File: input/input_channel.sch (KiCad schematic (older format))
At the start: 4 parts

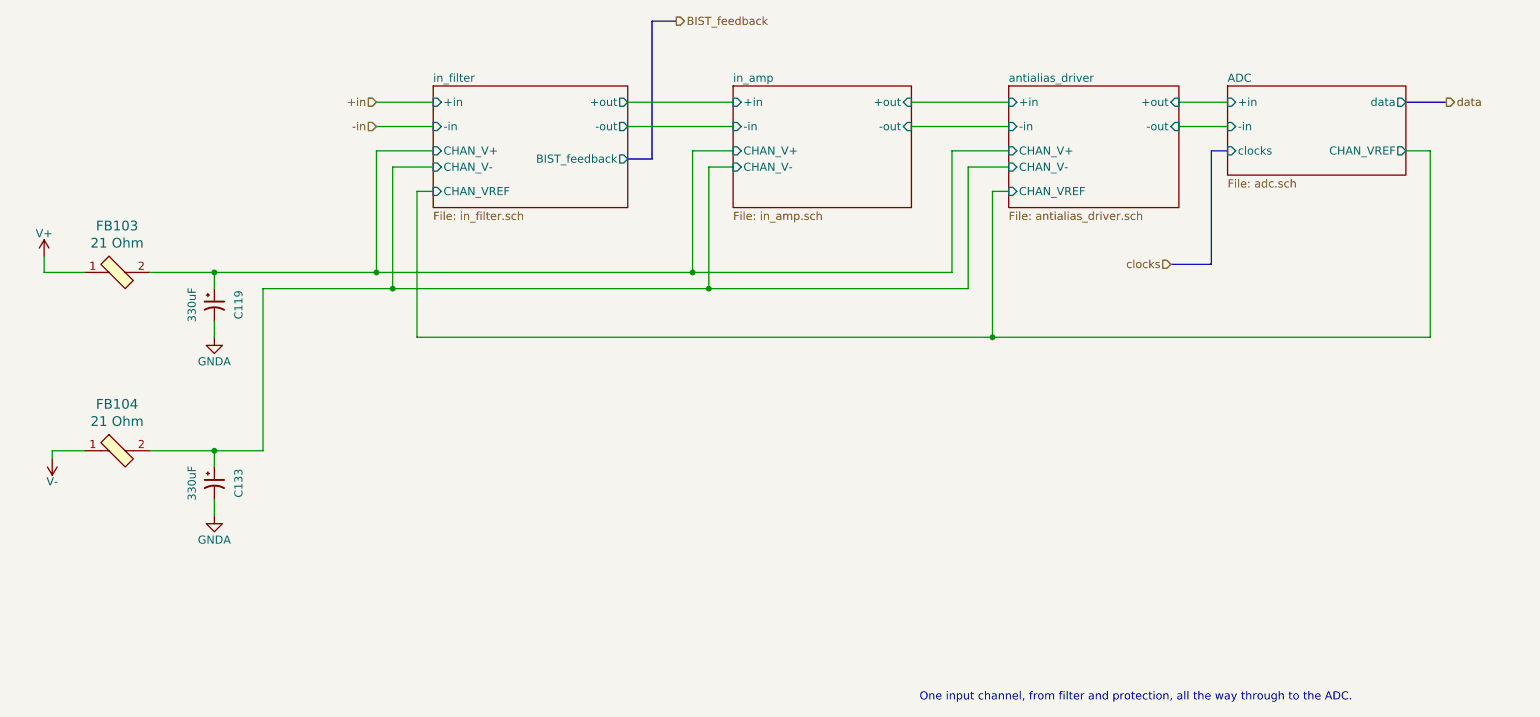
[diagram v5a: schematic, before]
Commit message: Cleanup to get ready to start board layout. I had to get rid off all the bus signals, since in Kicad busses don't work that way.  Added a couple testpoints; many more needed.
Work on component placement in PCB.  I changed DGND to plain GND and "protective earth" to
"earth" (for chassis ground).  Chassis ground is now connected on the board only via a capacitor.
I had to fix the connector footprint to match the pin numbers on the symbol (there was a case
difference).
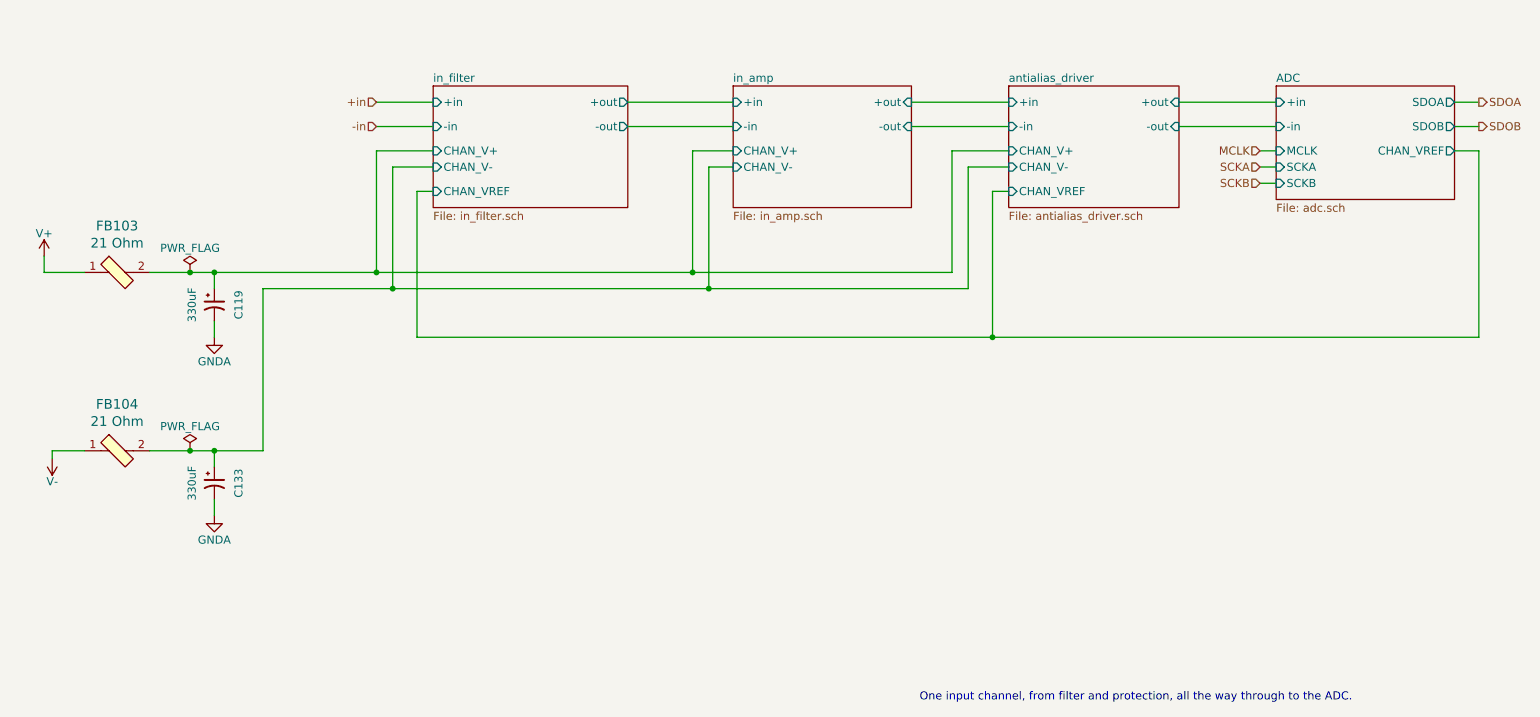
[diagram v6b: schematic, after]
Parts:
- FB103, FB104: footprint digikey-footprints:0805 -> Inductor_SMD:L_0805_2012Metric
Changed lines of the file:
@@
 F4 "-in" I L 4150 3200 50
 F5 "+in" I L 4150 3050 50
-F6 "BIST_feedback" O R 5350 3400 50
-F7 "CHAN_V+" I L 4150 3350 50
-F8 "CHAN_V-" I L 4150 3450 50
-F9 "CHAN_VREF" I L 4150 3600 50
+F6 "CHAN_V+" I L 4150 3350 50
+F7 "CHAN_V-" I L 4150 3450 50
+F8 "CHAN_VREF" I L 4150 3600 50
 $EndSheet
 $Sheet
@@
 F7 "CHAN_V-" I L 6000 3450 50
 $EndSheet
-Wire Wire Line
-	8750 3200 9050 3200
-Wire Wire Line
-	8750 3050 9050 3050
-Text HLabel 10400 3050 2    50   Output ~ 0
-data
 Text HLabel 3800 3050 0    50   Input ~ 0
 +in
@@
 Wire Wire Line
 	3800 3200 4150 3200
-Text HLabel 8700 4050 0    50   Input ~ 0
-clocks
-Wire Bus Line
-	9050 3350 8950 3350
-Wire Bus Line
-	8950 3350 8950 4050
-Wire Bus Line
-	8950 4050 8700 4050
-Wire Bus Line
-	10150 3050 10400 3050
-Wire Bus Line
-	5350 3400 5500 3400
-Wire Bus Line
-	5500 3400 5500 2550
-Wire Bus Line
-	5500 2550 5650 2550
 Wire Wire Line
 	7100 3050 7700 3050
@@
 F 0 "FB103" H 2200 4387 60  0000 C CNN
 F 1 "21 Ohm" H 2200 4281 60  0000 C CNN
-F 2 "digikey-footprints:0805" H 2400 4300 60  0001 L CNN
+F 2 "Inductor_SMD:L_0805_2012Metric" H 2400 4300 60  0001 L CNN
 F 3 "https://www.yuden.co.jp/productdata/catalog/chipbeads01_e.pdf" H 2400 4400 60  0001 L CNN
 F 4 "HZ0805C202R-10" H 2400 4600 60  0001 L CNN "MPN"
@@
 $EndComp
 Wire Wire Line
-	2400 4100 2800 4100
+	2400 4100 2650 4100
 Wire Wire Line
 	2800 4100 2800 4200
@@
 F 0 "FB104" H 2200 5487 60  0000 C CNN
 F 1 "21 Ohm" H 2200 5381 60  0000 C CNN
-F 2 "digikey-footprints:0805" H 2400 5400 60  0001 L CNN
+F 2 "Inductor_SMD:L_0805_2012Metric" H 2400 5400 60  0001 L CNN
 F 3 "https://www.yuden.co.jp/productdata/catalog/chipbeads01_e.pdf" H 2400 5500 60  0001 L CNN
 F 4 "HZ0805C202R-10" H 2400 5700 60  0001 L CNN "MPN"
@@
 $EndComp
 Wire Wire Line
-	2400 5200 2800 5200
+	2400 5200 2650 5200
 Wire Wire Line
 	2800 5200 2800 5300
@@
 	7450 3450 7700 3450
 Connection ~ 2800 5200
-Text HLabel 5650 2550 2    50   Output ~ 0
-BIST_feedback
 Wire Wire Line
 	5750 3350 5750 4100
@@
 	3900 4200 5850 4200
 $Sheet
-S 9050 2950 1100 550
+S 9350 2950 1100 700
 U 5DA78AA2
 F0 "ADC" 50
 F1 "adc.sch" 50
-F2 "+in" I L 9050 3050 50
-F3 "-in" I L 9050 3200 50
-F4 "data" O R 10150 3050 50
-F5 "clocks" I L 9050 3350 50
-F6 "CHAN_VREF" O R 10150 3350 50
+F2 "+in" I L 9350 3050 50
+F3 "-in" I L 9350 3200 50
+F4 "CHAN_VREF" O R 10450 3350 50
+F5 "SDOA" O R 10450 3050 50
+F6 "SDOB" O R 10450 3200 50
+F7 "MCLK" I L 9350 3350 50
+F8 "SCKB" I L 9350 3550 50
+F9 "SCKA" I L 9350 3450 50
 $EndSheet
 Wire Wire Line
@@
 Connection ~ 5850 4200
 Wire Wire Line
-	10150 3350 10300 3350
-Wire Wire Line
-	10300 3350 10300 4500
+	10450 3350 10600 3350
+Wire Wire Line
+	10600 3350 10600 4500
 Wire Wire Line
 	7700 3600 7600 3600
@@
 Connection ~ 7600 4500
 Wire Wire Line
-	7600 4500 10300 4500
-Wire Wire Line
 	4150 3600 4050 3600
 Wire Wire Line
 	4050 3600 4050 4500
+$Comp
+L power:PWR_FLAG #FLG0103
+U 1 1 5E8B0766
+P 2650 4100
+F 0 "#FLG0103" H 2650 4175 50  0001 C CNN
+F 1 "PWR_FLAG" H 2650 4250 50  0000 C CNN
+F 2 "" H 2650 4100 50  0001 C CNN
+F 3 "~" H 2650 4100 50  0001 C CNN
+	1    2650 4100
+	1    0    0    -1
+$EndComp
+Connection ~ 2650 4100
+Wire Wire Line
+	2650 4100 2800 4100
+$Comp
+L power:PWR_FLAG #FLG0104
+U 1 1 5E8B104C
+P 2650 5200
+F 0 "#FLG0104" H 2650 5275 50  0001 C CNN
+F 1 "PWR_FLAG" H 2650 5350 50  0000 C CNN
+F 2 "" H 2650 5200 50  0001 C CNN
+F 3 "~" H 2650 5200 50  0001 C CNN
+	1    2650 5200
+	1    0    0    -1
+$EndComp
+Connection ~ 2650 5200
+Wire Wire Line
+	2650 5200 2800 5200
+Text HLabel 10600 3050 2    50   Output ~ 0
+SDOA
+Text HLabel 10600 3200 2    50   Output ~ 0
+SDOB
+Text HLabel 9250 3350 0    50   Input ~ 0
+MCLK
+Text HLabel 9250 3550 0    50   Input ~ 0
+SCKB
+Text HLabel 9250 3450 0    50   Input ~ 0
+SCKA
+Wire Wire Line
+	10450 3050 10600 3050
+Wire Wire Line
+	10450 3200 10600 3200
+Wire Wire Line
+	9250 3350 9350 3350
+Wire Wire Line
+	9250 3450 9350 3450
+Wire Wire Line
+	9250 3550 9350 3550
+Wire Wire Line
+	8750 3200 9350 3200
+Wire Wire Line
+	8750 3050 9350 3050
+Wire Wire Line
+	7600 4500 10600 4500
 $EndSCHEMATC

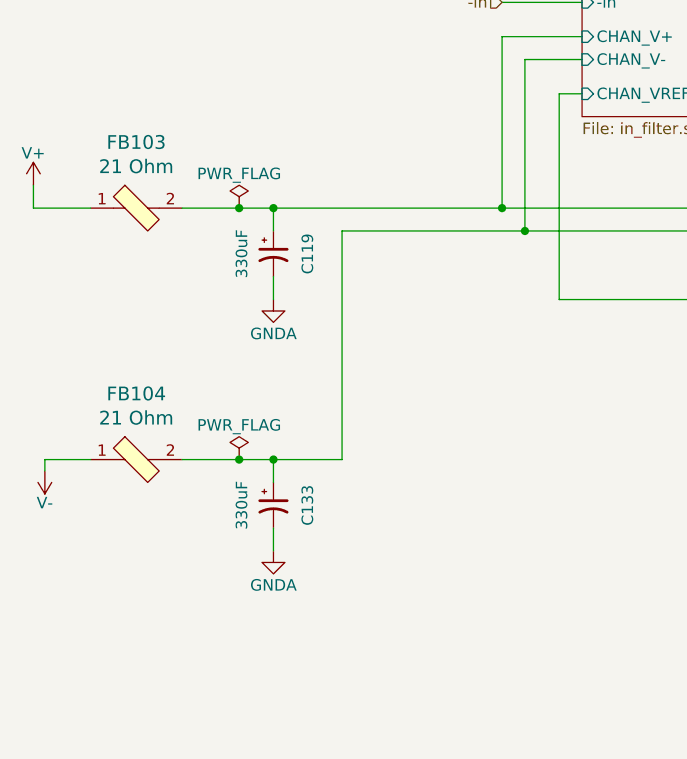
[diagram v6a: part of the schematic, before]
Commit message: Progress on input board layout.  Have adopted 100x280mm eurocard format with connector at the back. Schematic changes are mostly cosmetic.  The working board file is now input/input_board_rear.kicad_pcb
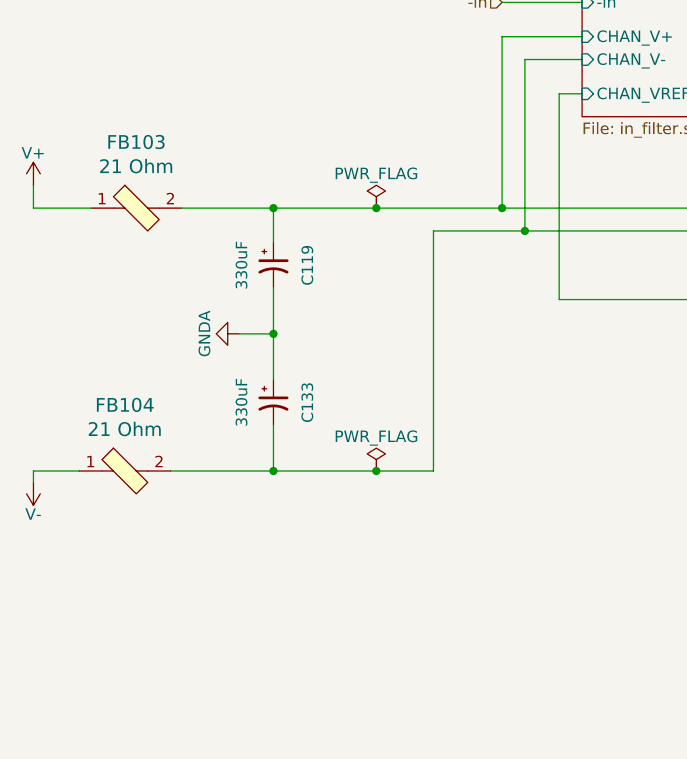
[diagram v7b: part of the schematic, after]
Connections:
- net GNDA: now also C133.1; no longer C133.2
- net antialias_driver/CHAN_V-: now also C133.2; no longer C133.1
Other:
- moved on the sheet: C119, C133, FB104
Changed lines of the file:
@@
 L ilemt_input:V- #PWR0121
 U 1 1 5E23B186
-P 1800 5350
-F 0 "#PWR0121" H 1800 5200 50  0001 C CNN
-F 1 "V-" H 1800 5310 50  0000 C CNN
-F 2 "" H 1800 5450 50  0001 C CNN
-F 3 "" H 1800 5450 50  0001 C CNN
-	1    1800 5350
+P 1750 5400
+F 0 "#PWR0121" H 1750 5250 50  0001 C CNN
+F 1 "V-" H 1750 5360 50  0000 C CNN
+F 2 "" H 1750 5500 50  0001 C CNN
+F 3 "" H 1750 5500 50  0001 C CNN
+	1    1750 5400
 	1    0    0    -1
 $EndComp
@@
 L Device:CP1_Small C?
 U 1 1 5E23EF6F
-P 2800 4300
+P 2800 4350
 AR Path="/5DFF6C0D/5E23EF6F" Ref="C?"  Part="1"
 AR Path="/5E1D6729/5E1DA2AA/5E23EF6F" Ref="C?"  Part="1"
@@
 AR Path="/5E51E83D/5E23EF6F" Ref="C?"  Part="1"
 AR Path="/5DFCF14D/5E23EF6F" Ref="C119"  Part="1"
-F 0 "C119" V 2950 4300 50  0000 C CNN
-F 1 "330uF" V 2662 4300 50  0000 C CNN
-F 2 "Capacitor_SMD:CP_Elec_8x6.7" H 2800 4300 50  0001 C CNN
-F 3 "~" H 2800 4300 50  0001 C CNN
-F 4 "16V aluminum solid polymer, ESR 22 mOhm" H 2800 4300 50  0001 C CNN "Description"
-F 5 "565-4285-1-ND" H 2800 4300 50  0001 C CNN "Digikey"
-F 6 "APXG160ARA331MH70G" H 2800 4300 50  0001 C CNN "MPN"
-	1    2800 4300
-	1    0    0    -1
-$EndComp
-Wire Wire Line
-	2400 4100 2650 4100
-Wire Wire Line
-	2800 4100 2800 4200
+F 0 "C119" V 2950 4350 50  0000 C CNN
+F 1 "330uF" V 2662 4350 50  0000 C CNN
+F 2 "Capacitor_SMD:CP_Elec_8x6.7" H 2800 4350 50  0001 C CNN
+F 3 "~" H 2800 4350 50  0001 C CNN
+F 4 "16V aluminum solid polymer, ESR 22 mOhm" H 2800 4350 50  0001 C CNN "Description"
+F 5 "565-4285-1-ND" H 2800 4350 50  0001 C CNN "Digikey"
+F 6 "APXG160ARA331MH70G" H 2800 4350 50  0001 C CNN "MPN"
+	1    2800 4350
+	1    0    0    -1
+$EndComp
+Wire Wire Line
+	2800 4100 2800 4250
 $Comp
 L power:GNDA #PWR0122
 U 1 1 5E23FC8E
-P 2800 4500
-F 0 "#PWR0122" H 2800 4250 50  0001 C CNN
-F 1 "GNDA" H 2800 4350 50  0000 C CNN
-F 2 "" H 2800 4500 50  0001 C CNN
-F 3 "" H 2800 4500 50  0001 C CNN
-	1    2800 4500
-	1    0    0    -1
-$EndComp
-Wire Wire Line
-	2800 4500 2800 4400
+P 2650 4650
+F 0 "#PWR0122" H 2650 4400 50  0001 C CNN
+F 1 "GNDA" H 2650 4500 50  0000 C CNN
+F 2 "" H 2650 4650 50  0001 C CNN
+F 3 "" H 2650 4650 50  0001 C CNN
+	1    2650 4650
+	0    1    1    0
+$EndComp
 $Comp
 L dk_Ferrite-Beads-and-Chips:MPZ2012S601AT000 FB?
 U 1 1 5E24179B
-P 2200 5200
+P 2150 5250
 AR Path="/5DFCF14D/5DE42731/5E24179B" Ref="FB?"  Part="1"
 AR Path="/5DFCF14D/5E24179B" Ref="FB104"  Part="1"
-F 0 "FB104" H 2200 5487 60  0000 C CNN
-F 1 "21 Ohm" H 2200 5381 60  0000 C CNN
-F 2 "Inductor_SMD:L_0805_2012Metric" H 2400 5400 60  0001 L CNN
-F 3 "https://www.yuden.co.jp/productdata/catalog/chipbeads01_e.pdf" H 2400 5500 60  0001 L CNN
-F 4 "HZ0805C202R-10" H 2400 5700 60  0001 L CNN "MPN"
-F 5 "Ferrite Beads and Chips" H 2400 5900 60  0001 L CNN "Family"
-F 6 "FERRITE BEAD 21 OHM 0805, 100 nH, 5 mOhm" H 2400 6200 60  0001 L CNN "Description"
-F 7 "587-1765-1-ND" H 2200 5200 50  0001 C CNN "Digikey"
-	1    2200 5200
+F 0 "FB104" H 2150 5537 60  0000 C CNN
+F 1 "21 Ohm" H 2150 5431 60  0000 C CNN
+F 2 "Inductor_SMD:L_0805_2012Metric" H 2350 5450 60  0001 L CNN
+F 3 "https://www.yuden.co.jp/productdata/catalog/chipbeads01_e.pdf" H 2350 5550 60  0001 L CNN
+F 4 "HZ0805C202R-10" H 2350 5750 60  0001 L CNN "MPN"
+F 5 "Ferrite Beads and Chips" H 2350 5950 60  0001 L CNN "Family"
+F 6 "FERRITE BEAD 21 OHM 0805, 100 nH, 5 mOhm" H 2350 6250 60  0001 L CNN "Description"
+F 7 "587-1765-1-ND" H 2150 5250 50  0001 C CNN "Digikey"
+	1    2150 5250
 	1    0    0    -1
 $EndComp
@@
 L Device:CP1_Small C?
 U 1 1 5E2417A1
-P 2800 5400
+P 2800 4950
 AR Path="/5DFF6C0D/5E2417A1" Ref="C?"  Part="1"
 AR Path="/5E1D6729/5E1DA2AA/5E2417A1" Ref="C?"  Part="1"
@@
 AR Path="/5E51E83D/5E2417A1" Ref="C?"  Part="1"
 AR Path="/5DFCF14D/5E2417A1" Ref="C133"  Part="1"
-F 0 "C133" V 2950 5400 50  0000 C CNN
-F 1 "330uF" V 2662 5400 50  0000 C CNN
-F 2 "Capacitor_SMD:CP_Elec_8x6.7" H 2800 5400 50  0001 C CNN
-F 3 "~" H 2800 5400 50  0001 C CNN
-F 4 "16V aluminum solid polymer, ESR 22 mOhm" H 2800 5400 50  0001 C CNN "Description"
-F 5 "565-4285-1-ND" H 2800 5400 50  0001 C CNN "Digikey"
-F 6 "APXG160ARA331MH70G" H 2800 5400 50  0001 C CNN "MPN"
-	1    2800 5400
-	1    0    0    -1
-$EndComp
-Wire Wire Line
-	2400 5200 2650 5200
-Wire Wire Line
-	2800 5200 2800 5300
-$Comp
-L power:GNDA #PWR0129
-U 1 1 5E2417A9
-P 2800 5600
-F 0 "#PWR0129" H 2800 5350 50  0001 C CNN
-F 1 "GNDA" H 2800 5450 50  0000 C CNN
-F 2 "" H 2800 5600 50  0001 C CNN
-F 3 "" H 2800 5600 50  0001 C CNN
-	1    2800 5600
-	1    0    0    -1
-$EndComp
-Wire Wire Line
-	2800 5600 2800 5500
-Wire Wire Line
-	2000 5200 1800 5200
-Wire Wire Line
-	1800 5200 1800 5250
-Wire Wire Line
-	2800 4100 3800 4100
+F 0 "C133" V 2950 4950 50  0000 C CNN
+F 1 "330uF" V 2662 4950 50  0000 C CNN
+F 2 "Capacitor_SMD:CP_Elec_8x6.7" H 2800 4950 50  0001 C CNN
+F 3 "~" H 2800 4950 50  0001 C CNN
+F 4 "16V aluminum solid polymer, ESR 22 mOhm" H 2800 4950 50  0001 C CNN "Description"
+F 5 "565-4285-1-ND" H 2800 4950 50  0001 C CNN "Digikey"
+F 6 "APXG160ARA331MH70G" H 2800 4950 50  0001 C CNN "MPN"
+	1    2800 4950
+	1    0    0    -1
+$EndComp
+Wire Wire Line
+	1950 5250 1750 5250
+Wire Wire Line
+	1750 5250 1750 5300
+Wire Wire Line
+	2800 4100 3250 4100
 Wire Wire Line
 	7350 4100 7350 3350
@@
 Connection ~ 2800 4100
 Wire Wire Line
-	2800 5200 3100 5200
-Wire Wire Line
-	3100 5200 3100 4200
-Wire Wire Line
-	3100 4200 3900 4200
-Wire Wire Line
 	7450 4200 7450 3450
 Wire Wire Line
 	7450 3450 7700 3450
-Connection ~ 2800 5200
 Wire Wire Line
 	5750 3350 5750 4100
@@
 L power:PWR_FLAG #FLG0103
 U 1 1 5E8B0766
-P 2650 4100
-F 0 "#FLG0103" H 2650 4175 50  0001 C CNN
-F 1 "PWR_FLAG" H 2650 4250 50  0000 C CNN
-F 2 "" H 2650 4100 50  0001 C CNN
-F 3 "~" H 2650 4100 50  0001 C CNN
-	1    2650 4100
-	1    0    0    -1
-$EndComp
-Connection ~ 2650 4100
-Wire Wire Line
-	2650 4100 2800 4100
-$Comp
-L power:PWR_FLAG #FLG0104
-U 1 1 5E8B104C
-P 2650 5200
-F 0 "#FLG0104" H 2650 5275 50  0001 C CNN
-F 1 "PWR_FLAG" H 2650 5350 50  0000 C CNN
-F 2 "" H 2650 5200 50  0001 C CNN
-F 3 "~" H 2650 5200 50  0001 C CNN
-	1    2650 5200
-	1    0    0    -1
-$EndComp
-Connection ~ 2650 5200
-Wire Wire Line
-	2650 5200 2800 5200
+P 3250 4100
+F 0 "#FLG0103" H 3250 4175 50  0001 C CNN
+F 1 "PWR_FLAG" H 3250 4250 50  0000 C CNN
+F 2 "" H 3250 4100 50  0001 C CNN
+F 3 "~" H 3250 4100 50  0001 C CNN
+	1    3250 4100
+	1    0    0    -1
+$EndComp
 Text HLabel 10600 3050 2    50   Output ~ 0
 SDOA
@@
 Wire Wire Line
 	7600 4500 10600 4500
+Wire Wire Line
+	2800 4450 2800 4650
+Wire Wire Line
+	3500 4200 3900 4200
+Wire Wire Line
+	2650 4650 2800 4650
+Connection ~ 2800 4650
+Wire Wire Line
+	2800 4650 2800 4850
+Wire Wire Line
+	3500 4200 3500 5250
+Connection ~ 3250 4100
+Wire Wire Line
+	3250 4100 3800 4100
+Wire Wire Line
+	2400 4100 2800 4100
+Wire Wire Line
+	2350 5250 2800 5250
+Connection ~ 2800 5250
+Wire Wire Line
+	2800 5250 2800 5050
+Wire Wire Line
+	3250 5250 3500 5250
+Wire Wire Line
+	2800 5250 3250 5250
+Connection ~ 3250 5250
+$Comp
+L power:PWR_FLAG #FLG0104
+U 1 1 5E8B104C
+P 3250 5250
+F 0 "#FLG0104" H 3250 5325 50  0001 C CNN
+F 1 "PWR_FLAG" H 3250 5400 50  0000 C CNN
+F 2 "" H 3250 5250 50  0001 C CNN
+F 3 "~" H 3250 5250 50  0001 C CNN
+	1    3250 5250
+	1    0    0    -1
+$EndComp
 $EndSCHEMATC

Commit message: Checkpoint before starting routing.  Added power and ground testpoints.
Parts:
- C119, C133: DK line (none) -> 19
- FB103, FB104: DK line (none) -> 24
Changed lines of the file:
@@
 EESchema Schematic File Version 4
-LIBS:input_board-cache
-EELAYER 29 0
+EELAYER 30 0
 EELAYER END
 $Descr A4 11693 8268
@@
 F 6 "FERRITE BEAD 21 OHM 0805, 100 nH, 5 mOhm" H 2400 5100 60  0001 L CNN "Description"
 F 7 "587-1765-1-ND" H 2200 4100 50  0001 C CNN "Digikey"
+F 8 "24" H 2200 4100 50  0001 C CNN "DK line"
 	1    2200 4100
 	1    0    0    -1
@@
 F 1 "330uF" V 2662 4350 50  0000 C CNN
 F 2 "Capacitor_SMD:CP_Elec_8x6.7" H 2800 4350 50  0001 C CNN
-F 3 "~" H 2800 4350 50  0001 C CNN
+F 3 "http://www.chemi-con.co.jp/cgi-bin/CAT_DB/SEARCH/cat_db_al.cgi?e=e&j=p&pdfname=pxg" H 2800 4350 50  0001 C CNN
 F 4 "16V aluminum solid polymer, ESR 22 mOhm" H 2800 4350 50  0001 C CNN "Description"
 F 5 "565-4285-1-ND" H 2800 4350 50  0001 C CNN "Digikey"
 F 6 "APXG160ARA331MH70G" H 2800 4350 50  0001 C CNN "MPN"
+F 7 "19" H 2800 4350 50  0001 C CNN "DK line"
 	1    2800 4350
 	1    0    0    -1
@@
 F 6 "FERRITE BEAD 21 OHM 0805, 100 nH, 5 mOhm" H 2350 6250 60  0001 L CNN "Description"
 F 7 "587-1765-1-ND" H 2150 5250 50  0001 C CNN "Digikey"
+F 8 "24" H 2150 5250 50  0001 C CNN "DK line"
 	1    2150 5250
 	1    0    0    -1
@@
 F 1 "330uF" V 2662 4950 50  0000 C CNN
 F 2 "Capacitor_SMD:CP_Elec_8x6.7" H 2800 4950 50  0001 C CNN
-F 3 "~" H 2800 4950 50  0001 C CNN
+F 3 "http://www.chemi-con.co.jp/cgi-bin/CAT_DB/SEARCH/cat_db_al.cgi?e=e&j=p&pdfname=pxg" H 2800 4950 50  0001 C CNN
 F 4 "16V aluminum solid polymer, ESR 22 mOhm" H 2800 4950 50  0001 C CNN "Description"
 F 5 "565-4285-1-ND" H 2800 4950 50  0001 C CNN "Digikey"
 F 6 "APXG160ARA331MH70G" H 2800 4950 50  0001 C CNN "MPN"
+F 7 "19" H 2800 4950 50  0001 C CNN "DK line"
 	1    2800 4950
 	1    0    0    -1
